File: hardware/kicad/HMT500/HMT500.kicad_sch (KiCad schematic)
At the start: 0 parts

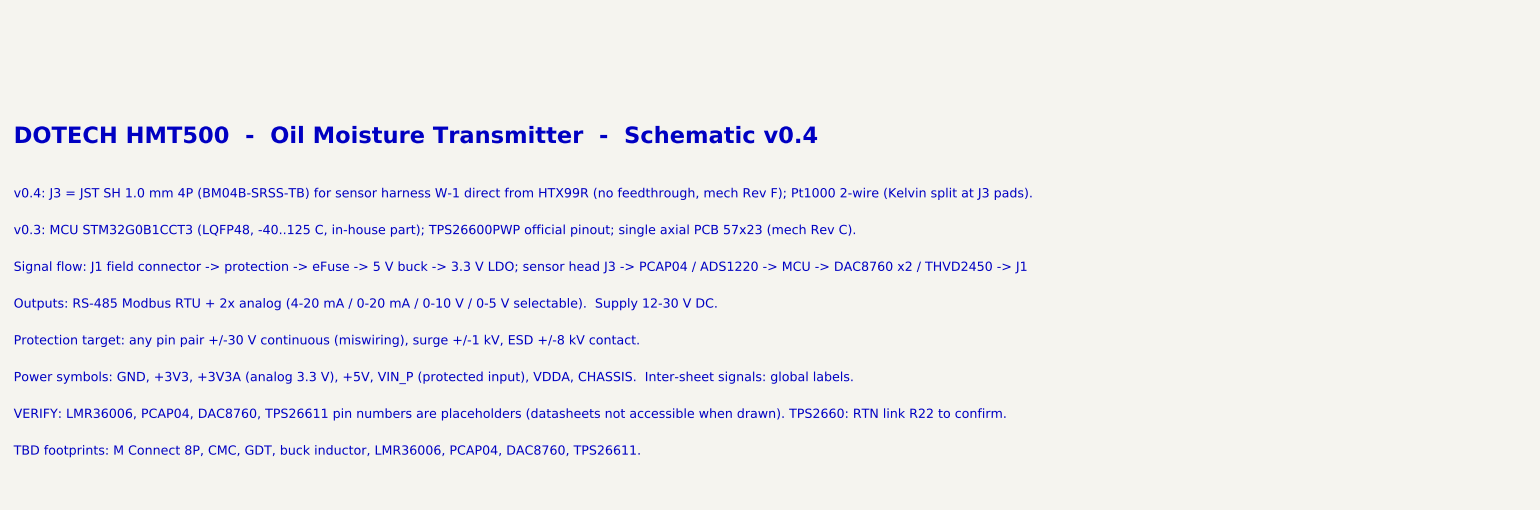
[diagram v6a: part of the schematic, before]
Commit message: M12 field harness W-2 with JST GH 8P, epoxy-molded pass-through
- Schematic v0.5: J1 = JST GH 1.25 mm 8P side entry (SM08B-GHS-TB), pin n =
  M12 pin n; J5 chassis spring contact replaces the M12 shell pin (68 nets, 0 errors)
- Mech: J1 at PCB x 52.5-58.5 facing the connector, harness W-2 (PTFE AWG28, 60 mm)
  and plug in CAD/drawings (item 18, note 10); output-zone parts rearranged
- 7 mm pass-through filled with epoxy over its full length after the cable is in
  (item 5, primary barrier)
- Parts list, KiCad board zones, RFQ, docs, decision log #18 and tests updated

Co-Authored-By: Claude Opus 5.5 <noreply@anthropic.com>
Claude-Session: https://claude.ai/code/session_01JA2o8uJsqp9Vzsg4b665ev
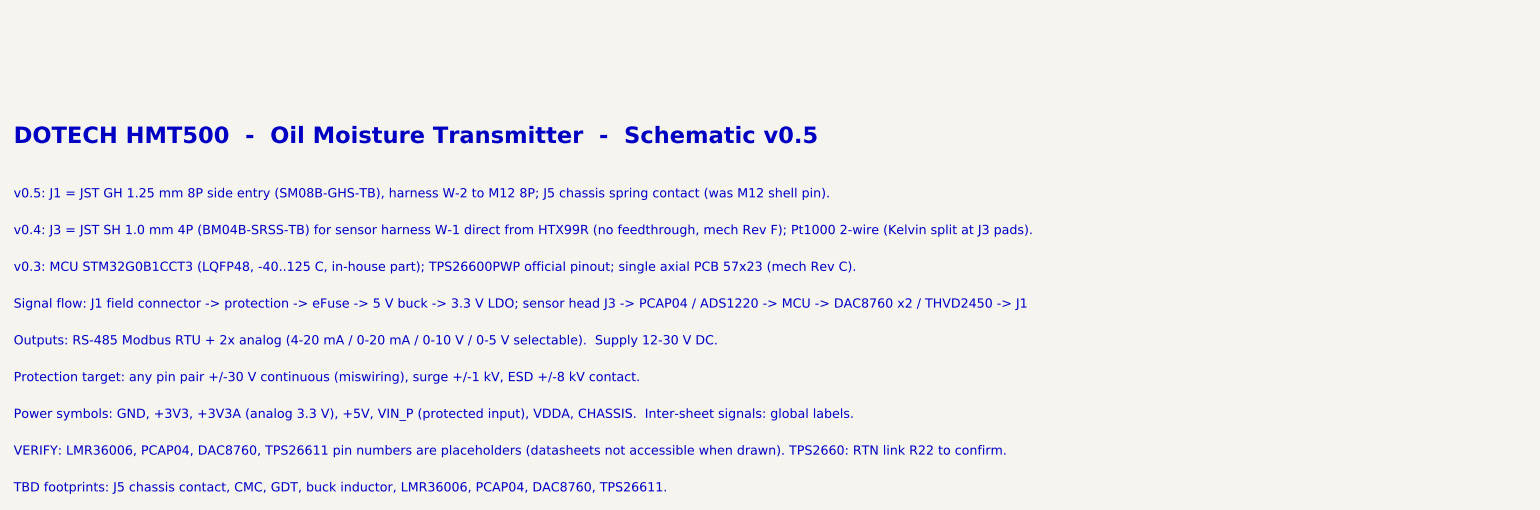
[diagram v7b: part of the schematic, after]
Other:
- note added: "DOTECH HMT500 - Oil Moisture Transmitter - Schematic v0.5"
- note added: "TBD footprints: J5 chassis contact, CMC, GDT, buck inductor, LMR36006, PCAP04, DAC8760, TPS26611."
- note added: "v0.5: J1 = JST GH 1.25 mm 8P side entry (SM08B-GHS-TB), harness W-2 to M12 8P; J5 chassis spring contact (was M12 shell pin)."
- note removed: "DOTECH HMT500 - Oil Moisture Transmitter - Schematic v0.4"
- note removed: "TBD footprints: M Connect 8P, CMC, GDT, buck inductor, LMR36006, PCAP04, DAC8760, TPS26611."
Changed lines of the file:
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@@
 (kicad_sch (version 20230121) (generator eeschema) (paper "A3")
-(title_block (title "HMT500  Top") (date "2026-09-29") (rev "0.4") (company "DOTECH Co., Ltd.") (comment 1 "Oil moisture transmitter HMT500 - RS-485 + 2x V/I analog output") (comment 2 "Design notes: docs/hw/circuit-design.md") (comment 3 "VERIFY=YES parts: pin numbers LMR36006/PCAP04/DAC8760/TPS26611; TPS2660 R22"))
+(title_block (title "HMT500  Top") (date "2026-09-29") (rev "0.5") (company "DOTECH Co., Ltd.") (comment 1 "Oil moisture transmitter HMT500 - RS-485 + 2x V/I analog output") (comment 2 "Design notes: docs/hw/circuit-design.md") (comment 3 "VERIFY=YES parts: pin numbers LMR36006/PCAP04/DAC8760/TPS26611; TPS2660 R22"))
 (sheet (at 30.48 55.88) (size 106.68 45.72) (fields_autoplaced) (stroke (width 0.1524) (type solid)) (fill (color 0 0 0 0.0000)) (property "Sheetname" "1. Connector & input protection" (at 30.48 55.118 0) (effects (font (size 1.8 1.8) bold) (justify left bottom))) (property "Sheetfile" "connector.kicad_sch" (at 30.48 102.362 0) (effects (font (size 1.27 1.27)) (justify left top))) (instances (project "HMT500" (path "/1ebb025b-11bd-5f7c-aaab-41e2a750e8b3" (page "2")))))
 (text "Field connector, 2-stage bidirectional TVS surge protection, chassis isolation" (at 33.02 78.74 0) (effects (font (size 1.4 1.4)) (justify left bottom)))
@@
 (sheet (at 284.48 132.08) (size 106.68 45.72) (fields_autoplaced) (stroke (width 0.1524) (type solid)) (fill (color 0 0 0 0.0000)) (property "Sheetname" "6. RS-485" (at 284.48 131.318 0) (effects (font (size 1.8 1.8) bold) (justify left bottom))) (property "Sheetfile" "rs485.kicad_sch" (at 284.48 178.562 0) (effects (font (size 1.27 1.27)) (justify left top))) (instances (project "HMT500" (path "/1ebb025b-11bd-5f7c-aaab-41e2a750e8b3" (page "7")))))
 (text "THVD2450 +/-70V fault-protected transceiver" (at 287.02 154.94 0) (effects (font (size 1.4 1.4)) (justify left bottom)))
-(text "DOTECH HMT500  -  Oil Moisture Transmitter  -  Schematic v0.4" (at 30.48 223.52 0) (effects (font (size 2.5 2.5) bold) (justify left bottom)))
-(text "v0.4: J3 = JST SH 1.0 mm 4P (BM04B-SRSS-TB) for sensor harness W-1 direct from HTX99R (no feedthrough, mech Rev F); Pt1000 2-wire (Kelvin split at J3 pads)." (at 30.48 231.648 0) (effects (font (size 1.4 1.4)) (justify left bottom)))
-(text "v0.3: MCU STM32G0B1CCT3 (LQFP48, -40..125 C, in-house part); TPS26600PWP official pinout; single axial PCB 57x23 (mech Rev C)." (at 30.48 237.236 0) (effects (font (size 1.4 1.4)) (justify left bottom)))
-(text "Signal flow: J1 field connector -> protection -> eFuse -> 5 V buck -> 3.3 V LDO; sensor head J3 -> PCAP04 / ADS1220 -> MCU -> DAC8760 x2 / THVD2450 -> J1" (at 30.48 242.824 0) (effects (font (size 1.4 1.4)) (justify left bottom)))
-(text "Outputs: RS-485 Modbus RTU + 2x analog (4-20 mA / 0-20 mA / 0-10 V / 0-5 V selectable).  Supply 12-30 V DC." (at 30.48 248.412 0) (effects (font (size 1.4 1.4)) (justify left bottom)))
-(text "Protection target: any pin pair +/-30 V continuous (miswiring), surge +/-1 kV, ESD +/-8 kV contact." (at 30.48 254 0) (effects (font (size 1.4 1.4)) (justify left bottom)))
-(text "Power symbols: GND, +3V3, +3V3A (analog 3.3 V), +5V, VIN_P (protected input), VDDA, CHASSIS.  Inter-sheet signals: global labels." (at 30.48 259.588 0) (effects (font (size 1.4 1.4)) (justify left bottom)))
-(text "VERIFY: LMR36006, PCAP04, DAC8760, TPS26611 pin numbers are placeholders (datasheets not accessible when drawn). TPS2660: RTN link R22 to confirm." (at 30.48 265.176 0) (effects (font (size 1.4 1.4)) (justify left bottom)))
-(text "TBD footprints: M Connect 8P, CMC, GDT, buck inductor, LMR36006, PCAP04, DAC8760, TPS26611." (at 30.48 270.764 0) (effects (font (size 1.4 1.4)) (justify left bottom)))
+(text "DOTECH HMT500  -  Oil Moisture Transmitter  -  Schematic v0.5" (at 30.48 223.52 0) (effects (font (size 2.5 2.5) bold) (justify left bottom)))
+(text "v0.5: J1 = JST GH 1.25 mm 8P side entry (SM08B-GHS-TB), harness W-2 to M12 8P; J5 chassis spring contact (was M12 shell pin)." (at 30.48 231.648 0) (effects (font (size 1.4 1.4)) (justify left bottom)))
+(text "v0.4: J3 = JST SH 1.0 mm 4P (BM04B-SRSS-TB) for sensor harness W-1 direct from HTX99R (no feedthrough, mech Rev F); Pt1000 2-wire (Kelvin split at J3 pads)." (at 30.48 237.236 0) (effects (font (size 1.4 1.4)) (justify left bottom)))
+(text "v0.3: MCU STM32G0B1CCT3 (LQFP48, -40..125 C, in-house part); TPS26600PWP official pinout; single axial PCB 57x23 (mech Rev C)." (at 30.48 242.824 0) (effects (font (size 1.4 1.4)) (justify left bottom)))
+(text "Signal flow: J1 field connector -> protection -> eFuse -> 5 V buck -> 3.3 V LDO; sensor head J3 -> PCAP04 / ADS1220 -> MCU -> DAC8760 x2 / THVD2450 -> J1" (at 30.48 248.412 0) (effects (font (size 1.4 1.4)) (justify left bottom)))
+(text "Outputs: RS-485 Modbus RTU + 2x analog (4-20 mA / 0-20 mA / 0-10 V / 0-5 V selectable).  Supply 12-30 V DC." (at 30.48 254 0) (effects (font (size 1.4 1.4)) (justify left bottom)))
+(text "Protection target: any pin pair +/-30 V continuous (miswiring), surge +/-1 kV, ESD +/-8 kV contact." (at 30.48 259.588 0) (effects (font (size 1.4 1.4)) (justify left bottom)))
+(text "Power symbols: GND, +3V3, +3V3A (analog 3.3 V), +5V, VIN_P (protected input), VDDA, CHASSIS.  Inter-sheet signals: global labels." (at 30.48 265.176 0) (effects (font (size 1.4 1.4)) (justify left bottom)))
+(text "VERIFY: LMR36006, PCAP04, DAC8760, TPS26611 pin numbers are placeholders (datasheets not accessible when drawn). TPS2660: RTN link R22 to confirm." (at 30.48 270.764 0) (effects (font (size 1.4 1.4)) (justify left bottom)))
+(text "TBD footprints: J5 chassis contact, CMC, GDT, buck inductor, LMR36006, PCAP04, DAC8760, TPS26611." (at 30.48 276.352 0) (effects (font (size 1.4 1.4)) (justify left bottom)))
 (sheet_instances (path "/" (page "1")))
 )

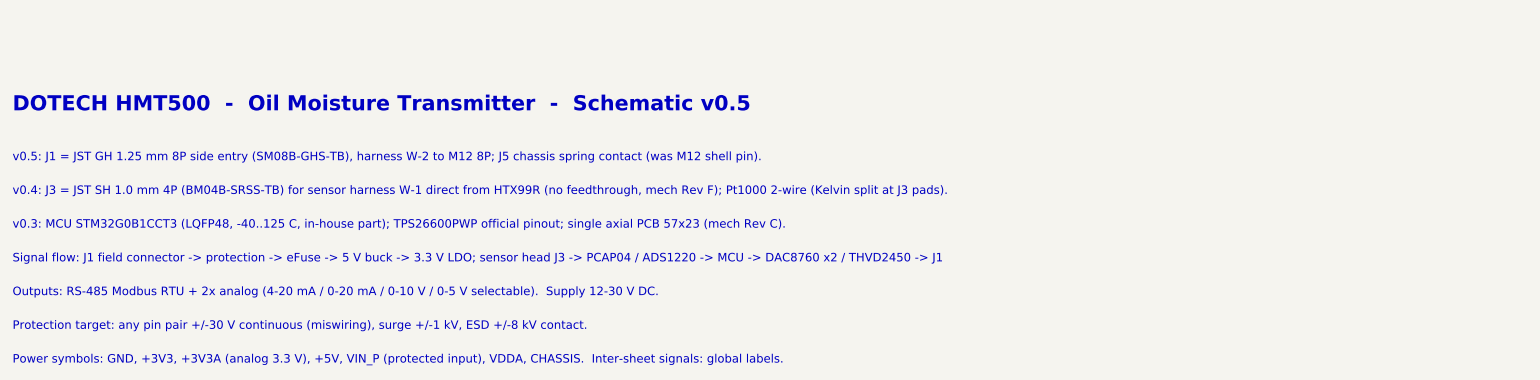
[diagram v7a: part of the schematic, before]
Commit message: J3 sensor header to right-angle JST SH SM04B-SRSS-TB
- Side entry facing the sensor (-x) at PCB x 22.5-26.5, height 2.95; W-1 plugs
  in straight from the holder hole with no bend
- PCAP04 / ADS1220 / Cref moved behind J3
- Schematic footprint, parts list, board zone label, CAD, drawings, renders,
  docs, decision log #19 and tests updated

Co-Authored-By: Claude Opus 5.5 <noreply@anthropic.com>
Claude-Session: https://claude.ai/code/session_01JA2o8uJsqp9Vzsg4b665ev
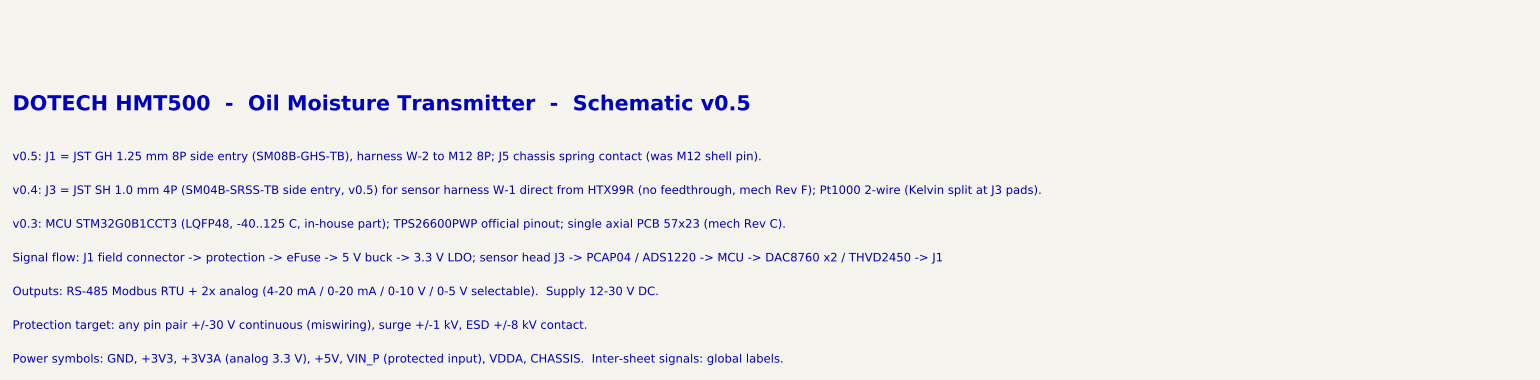
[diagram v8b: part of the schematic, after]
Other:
- note added: "v0.4: J3 = JST SH 1.0 mm 4P (SM04B-SRSS-TB side entry, v0.5) for sensor harness W-1 direct from HTX99R (no feedthrough, mech Rev F); Pt1000 2-wire (Kelvin split at J3 pads)."
- note removed: "v0.4: J3 = JST SH 1.0 mm 4P (BM04B-SRSS-TB) for sensor harness W-1 direct from HTX99R (no feedthrough, mech Rev F); Pt1000 2-wire (Kelvin split at J3 pads)."
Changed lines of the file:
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@@
 (text "DOTECH HMT500  -  Oil Moisture Transmitter  -  Schematic v0.5" (at 30.48 223.52 0) (effects (font (size 2.5 2.5) bold) (justify left bottom)))
 (text "v0.5: J1 = JST GH 1.25 mm 8P side entry (SM08B-GHS-TB), harness W-2 to M12 8P; J5 chassis spring contact (was M12 shell pin)." (at 30.48 231.648 0) (effects (font (size 1.4 1.4)) (justify left bottom)))
-(text "v0.4: J3 = JST SH 1.0 mm 4P (BM04B-SRSS-TB) for sensor harness W-1 direct from HTX99R (no feedthrough, mech Rev F); Pt1000 2-wire (Kelvin split at J3 pads)." (at 30.48 237.236 0) (effects (font (size 1.4 1.4)) (justify left bottom)))
+(text "v0.4: J3 = JST SH 1.0 mm 4P (SM04B-SRSS-TB side entry, v0.5) for sensor harness W-1 direct from HTX99R (no feedthrough, mech Rev F); Pt1000 2-wire (Kelvin split at J3 pads)." (at 30.48 237.236 0) (effects (font (size 1.4 1.4)) (justify left bottom)))
 (text "v0.3: MCU STM32G0B1CCT3 (LQFP48, -40..125 C, in-house part); TPS26600PWP official pinout; single axial PCB 57x23 (mech Rev C)." (at 30.48 242.824 0) (effects (font (size 1.4 1.4)) (justify left bottom)))
 (text "Signal flow: J1 field connector -> protection -> eFuse -> 5 V buck -> 3.3 V LDO; sensor head J3 -> PCAP04 / ADS1220 -> MCU -> DAC8760 x2 / THVD2450 -> J1" (at 30.48 248.412 0) (effects (font (size 1.4 1.4)) (justify left bottom)))
